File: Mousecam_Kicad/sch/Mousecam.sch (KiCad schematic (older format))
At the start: 16 parts, among them J1 Microsemi_FlashPro-JTAG-10, U1 TLV7103318DSER

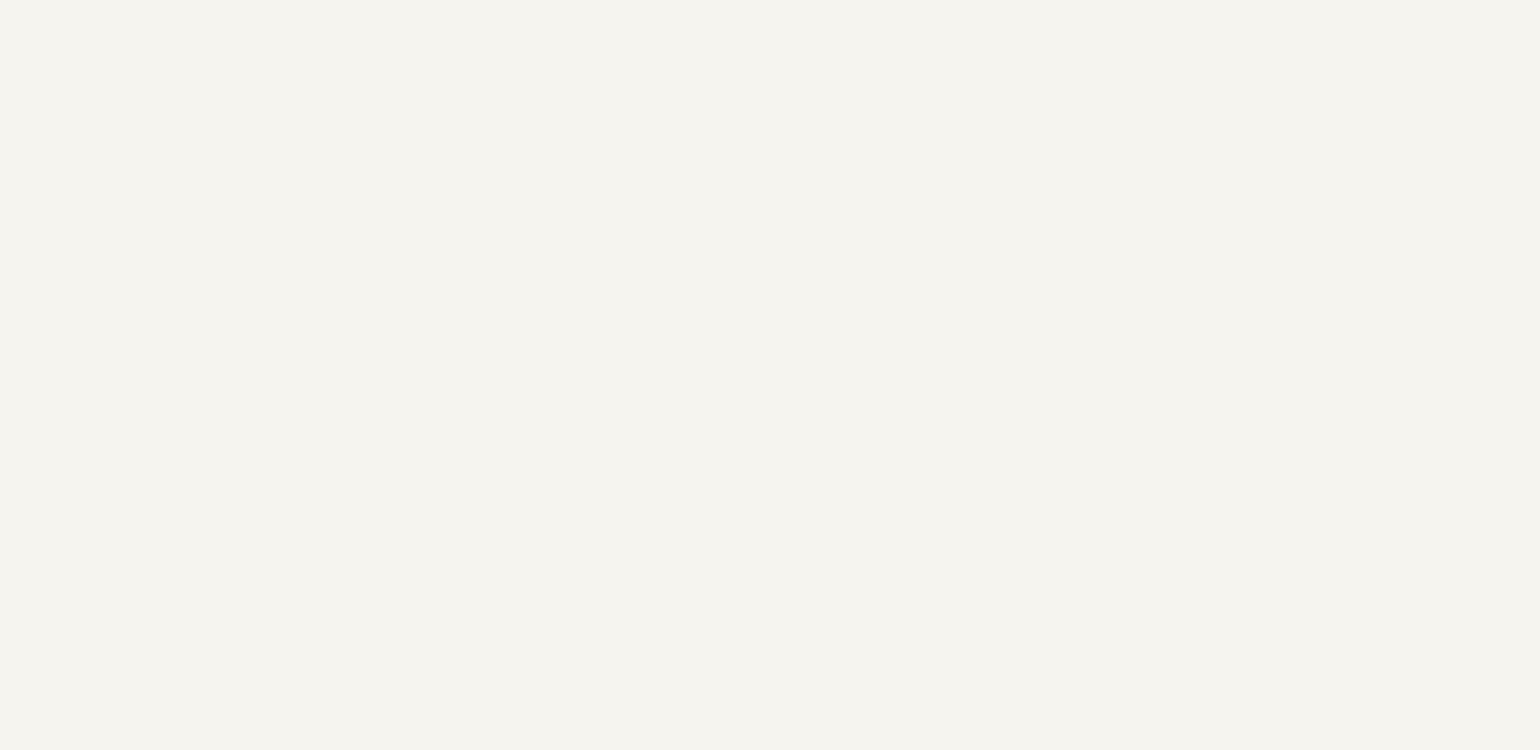
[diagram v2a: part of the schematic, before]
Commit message: updated relative path for libs
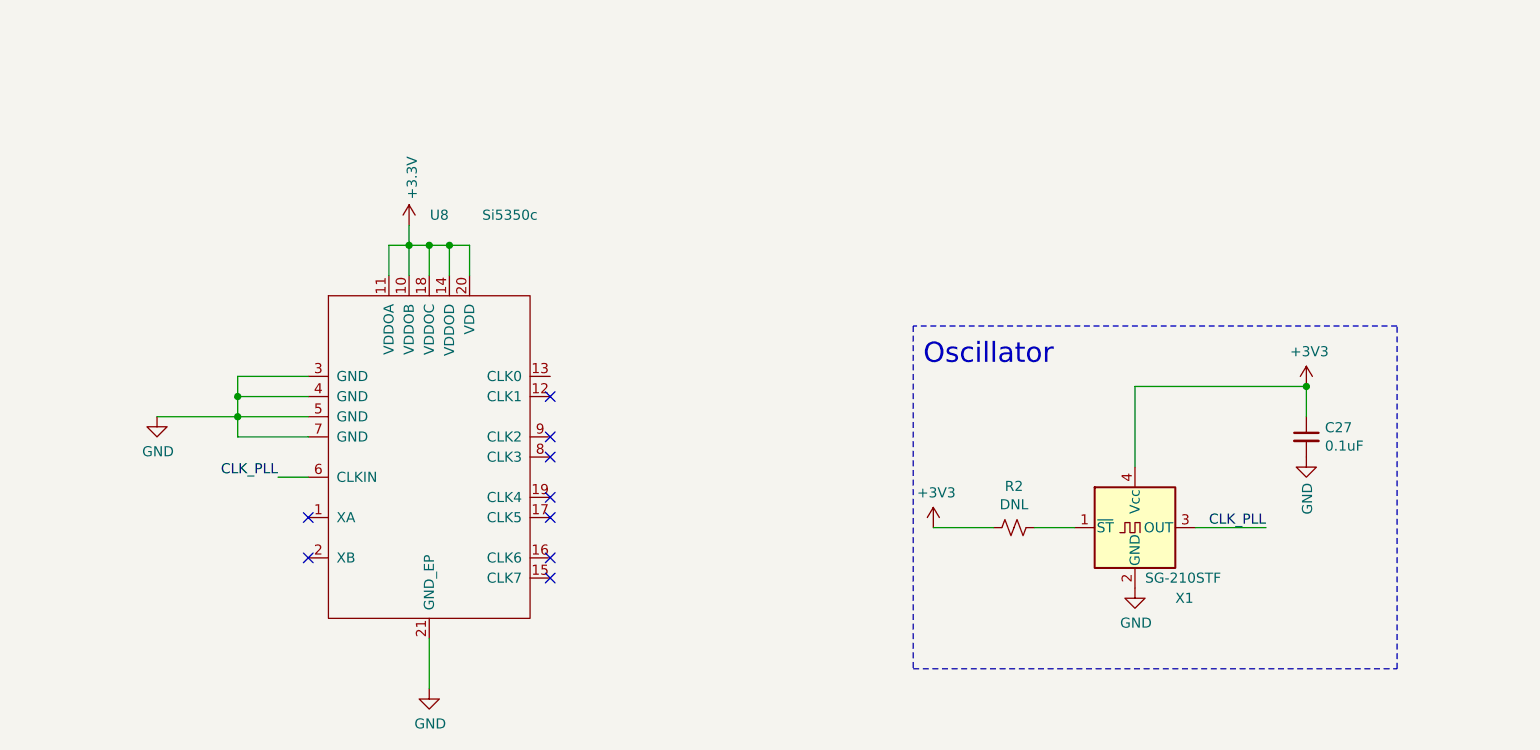
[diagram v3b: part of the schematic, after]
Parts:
- added C27: 0.1uF, Capacitor_SMD:C_0603_1608Metric_Pad1.05x0.95mm_HandSolder, symbol Device:C_Small
- added R2: DNL, Resistor_SMD:R_0603_1608Metric_Pad1.05x0.95mm_HandSolder, symbol Device:R_Small_US
- added U8: Si5350c, Si5350c:QFN50P300X300X60-21N, symbol Si5350c:Si5350c
- added X1: SG-210STF, Oscillator:Oscillator_SMD_SeikoEpson_SG210-4Pin_2.5x2.0mm, symbol Oscillator:SG-210STF
- R1, R3, R4: footprint (none) -> Resistor_SMD:R_0603_1608Metric_Pad1.05x0.95mm_HandSolder
- U1: footprint DSE6 -> TLV7103318DSER:TLV7103318DSER
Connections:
- net +3V3: now also C27.1, R2.2, U8.10 (VDDOB), U8.11 (VDDOA), U8.14 (VDDOD), U8.18 (VDDOC), U8.20 (VDD), X1.4 (Vcc)
- net GND: now also C27.2, U8.21 (GND_EP), U8.3 (GND), U8.4 (GND), U8.5 (GND), U8.7 (GND), X1.2 (GND)
- new net: R2.1, X1.1 (~ST~)
- new net CLK_PLL: U8.6 (CLKIN), X1.3 (OUT)
- no-connect marks 0 -> 9
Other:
- note added: "Oscillator"
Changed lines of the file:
@@
 F 0 "R1" H 7609 3446 50  0000 L CNN
 F 1 "10k" H 7609 3355 50  0000 L CNN
-F 2 "" H 7550 3400 50  0001 C CNN
+F 2 "Resistor_SMD:R_0603_1608Metric_Pad1.05x0.95mm_HandSolder" H 7550 3400 50  0001 C CNN
 F 3 "~" H 7550 3400 50  0001 C CNN
 	1    7550 3400
@@
 F 0 "R4" H 8009 3446 50  0000 L CNN
 F 1 "10k" H 8009 3355 50  0000 L CNN
-F 2 "" H 7950 3400 50  0001 C CNN
+F 2 "Resistor_SMD:R_0603_1608Metric_Pad1.05x0.95mm_HandSolder" H 7950 3400 50  0001 C CNN
 F 3 "~" H 7950 3400 50  0001 C CNN
 	1    7950 3400
@@
 F 0 "R3" H 7809 4346 50  0000 L CNN
 F 1 "1k" H 7809 4255 50  0000 L CNN
-F 2 "" H 7750 4300 50  0001 C CNN
+F 2 "Resistor_SMD:R_0603_1608Metric_Pad1.05x0.95mm_HandSolder" H 7750 4300 50  0001 C CNN
 F 3 "~" H 7750 4300 50  0001 C CNN
 	1    7750 4300
@@
 F 0 "U1" H 3450 1787 60  0000 C CNN
 F 1 "TLV7103318DSER" H 3450 1681 60  0000 C CNN
-F 2 "DSE6" H 3450 1650 60  0001 C CNN
+F 2 "TLV7103318DSER:TLV7103318DSER" H 3450 1650 60  0001 C CNN
 F 3 "" H 2800 1400 60  0000 C CNN
 	1    2800 1400
 	1    0    0    -1
 $EndComp
+$Comp
+L Si5350c:Si5350c U8
+U 1 1 608C5AF5
+P 3000 8700
+F 0 "U8" H 3050 9600 50  0000 C CNN
+F 1 "Si5350c" H 3400 9600 50  0000 C CNN
+F 2 "Si5350c:QFN50P300X300X60-21N" H 3000 8700 50  0001 C CNN
+F 3 "" H 3000 8700 50  0001 C CNN
+	1    3000 8700
+	1    0    0    -1
+$EndComp
+Wire Wire Line
+	2400 8600 2050 8600
+Wire Wire Line
+	2050 8600 2050 8700
+Wire Wire Line
+	2050 8900 2400 8900
+Wire Wire Line
+	2400 8800 2050 8800
+Connection ~ 2050 8800
+Wire Wire Line
+	2050 8800 2050 8900
+Wire Wire Line
+	2400 8700 2050 8700
+Connection ~ 2050 8700
+Wire Wire Line
+	2050 8700 2050 8800
+$Comp
+L power:GND #PWR0101
+U 1 1 608D08EB
+P 1650 8800
+F 0 "#PWR0101" H 1650 8550 50  0001 C CNN
+F 1 "GND" H 1655 8627 50  0000 C CNN
+F 2 "" H 1650 8800 50  0001 C CNN
+F 3 "" H 1650 8800 50  0001 C CNN
+	1    1650 8800
+	1    0    0    -1
+$EndComp
+Wire Wire Line
+	1650 8800 2050 8800
+Wire Notes Line
+	5400 10050 7800 10050
+Wire Notes Line
+	7800 10050 7800 8350
+Wire Notes Line
+	7800 8350 5400 8350
+Wire Notes Line
+	5400 8350 5400 10050
+$Comp
+L Oscillator:SG-210STF X?
+U 1 1 608ED851
+P 6500 9350
+AR Path="/607CBC7A/608ED851" Ref="X?"  Part="1"
+AR Path="/608ED851" Ref="X1"  Part="1"
+F 0 "X1" H 6700 9000 50  0000 L CNN
+F 1 "SG-210STF" H 6550 9100 50  0000 L CNN
+F 2 "Oscillator:Oscillator_SMD_SeikoEpson_SG210-4Pin_2.5x2.0mm" H 6950 9000 50  0001 C CNN
+F 3 "https://support.epson.biz/td/api/doc_check.php?mode=dl&lang=en&Parts=SG-210STF" H 6400 9350 50  0001 C CNN
+	1    6500 9350
+	1    0    0    -1
+$EndComp
+$Comp
+L power:+3V3 #PWR?
+U 1 1 608ED857
+P 5500 9350
+AR Path="/607CBC7A/608ED857" Ref="#PWR?"  Part="1"
+AR Path="/608ED857" Ref="#PWR0102"  Part="1"
+F 0 "#PWR0102" H 5500 9200 50  0001 C CNN
+F 1 "+3V3" H 5515 9523 50  0000 C CNN
+F 2 "" H 5500 9350 50  0001 C CNN
+F 3 "" H 5500 9350 50  0001 C CNN
+	1    5500 9350
+	1    0    0    -1
+$EndComp
+$Comp
+L Device:R_Small_US R?
+U 1 1 608ED85D
+P 5900 9350
+AR Path="/607CBC7A/608ED85D" Ref="R?"  Part="1"
+AR Path="/608ED85D" Ref="R2"  Part="1"
+F 0 "R2" V 5695 9350 50  0000 C CNN
+F 1 "DNL" V 5786 9350 50  0000 C CNN
+F 2 "Resistor_SMD:R_0603_1608Metric_Pad1.05x0.95mm_HandSolder" H 5900 9350 50  0001 C CNN
+F 3 "~" H 5900 9350 50  0001 C CNN
+	1    5900 9350
+	0    1    1    0
+$EndComp
+Wire Wire Line
+	6200 9350 6000 9350
+Wire Wire Line
+	5800 9350 5500 9350
+$Comp
+L power:GND #PWR?
+U 1 1 608ED865
+P 6500 9650
+AR Path="/607CBC7A/608ED865" Ref="#PWR?"  Part="1"
+AR Path="/608ED865" Ref="#PWR0103"  Part="1"
+F 0 "#PWR0103" H 6500 9400 50  0001 C CNN
+F 1 "GND" H 6505 9477 50  0000 C CNN
+F 2 "" H 6500 9650 50  0001 C CNN
+F 3 "" H 6500 9650 50  0001 C CNN
+	1    6500 9650
+	1    0    0    -1
+$EndComp
+Wire Wire Line
+	6800 9350 7150 9350
+Text Label 7150 9350 2    50   ~ 0
+CLK_PLL
+$Comp
+L power:GND #PWR?
+U 1 1 608ED86D
+P 7350 9000
+AR Path="/607CBC7A/608ED86D" Ref="#PWR?"  Part="1"
+AR Path="/608ED86D" Ref="#PWR0104"  Part="1"
+F 0 "#PWR0104" H 7350 8750 50  0001 C CNN
+F 1 "GND" V 7355 8872 50  0000 R CNN
+F 2 "" H 7350 9000 50  0001 C CNN
+F 3 "" H 7350 9000 50  0001 C CNN
+	1    7350 9000
+	1    0    0    -1
+$EndComp
+Text Notes 5450 8550 0    100  ~ 0
+Oscillator
+$Comp
+L power:+3V3 #PWR?
+U 1 1 608ED874
+P 7350 8650
+AR Path="/607CBC7A/608ED874" Ref="#PWR?"  Part="1"
+AR Path="/608ED874" Ref="#PWR0105"  Part="1"
+F 0 "#PWR0105" H 7350 8500 50  0001 C CNN
+F 1 "+3V3" H 7365 8823 50  0000 C CNN
+F 2 "" H 7350 8650 50  0001 C CNN
+F 3 "" H 7350 8650 50  0001 C CNN
+	1    7350 8650
+	1    0    0    -1
+$EndComp
+Wire Wire Line
+	6500 8650 6500 9050
+Wire Wire Line
+	6500 8650 7350 8650
+Wire Wire Line
+	7350 8800 7350 8650
+Connection ~ 7350 8650
+$Comp
+L Device:C_Small C?
+U 1 1 608ED87E
+P 7350 8900
+AR Path="/607CBDDC/608ED87E" Ref="C?"  Part="1"
+AR Path="/607CBC7A/608ED87E" Ref="C?"  Part="1"
+AR Path="/608ED87E" Ref="C27"  Part="1"
+F 0 "C27" H 7442 8946 50  0000 L CNN
+F 1 "0.1uF" H 7442 8855 50  0000 L CNN
+F 2 "Capacitor_SMD:C_0603_1608Metric_Pad1.05x0.95mm_HandSolder" H 7350 8900 50  0001 C CNN
+F 3 "~" H 7350 8900 50  0001 C CNN
+	1    7350 8900
+	1    0    0    -1
+$EndComp
+Wire Wire Line
+	3200 7950 3200 8100
+Wire Wire Line
+	3100 8100 3100 7950
+Connection ~ 3100 7950
+Wire Wire Line
+	3100 7950 3200 7950
+Wire Wire Line
+	3000 8100 3000 7950
+Connection ~ 3000 7950
+Wire Wire Line
+	3000 7950 3100 7950
+Wire Wire Line
+	2900 8100 2900 7950
+Connection ~ 2900 7950
+Wire Wire Line
+	2900 7950 3000 7950
+Wire Wire Line
+	2800 8100 2800 7950
+Wire Wire Line
+	2800 7950 2900 7950
+$Comp
+L power:GND #PWR0106
+U 1 1 6090EEAB
+P 3000 10150
+F 0 "#PWR0106" H 3000 9900 50  0001 C CNN
+F 1 "GND" H 3005 9977 50  0000 C CNN
+F 2 "" H 3000 10150 50  0001 C CNN
+F 3 "" H 3000 10150 50  0001 C CNN
+	1    3000 10150
+	1    0    0    -1
+$EndComp
+Wire Wire Line
+	3000 10150 3000 9900
+$Comp
+L power:+3.3V #PWR?
+U 1 1 6092631B
+P 2900 7850
+AR Path="/607CBDDC/6092631B" Ref="#PWR?"  Part="1"
+AR Path="/6092631B" Ref="#PWR0107"  Part="1"
+F 0 "#PWR0107" H 2900 7700 50  0001 C CNN
+F 1 "+3.3V" V 2915 7978 50  0000 L CNN
+F 2 "" H 2900 7850 50  0001 C CNN
+F 3 "" H 2900 7850 50  0001 C CNN
+	1    2900 7850
+	1    0    0    -1
+$EndComp
+Wire Wire Line
+	2900 7850 2900 7950
+NoConn ~ 2400 9300
+NoConn ~ 2400 9500
+NoConn ~ 3600 8700
+NoConn ~ 3600 8900
+NoConn ~ 3600 9000
+NoConn ~ 3600 9200
+NoConn ~ 3600 9300
+NoConn ~ 3600 9500
+NoConn ~ 3600 9600
+Text Label 2250 9100 2    50   ~ 0
+CLK_PLL
+Wire Wire Line
+	2250 9100 2400 9100
 $EndSCHEMATC
